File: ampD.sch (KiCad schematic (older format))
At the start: 13 parts, among them U10 Mux, U11 screw_term, U6 TL084, U9 screw_term

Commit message: changed to mcp6004 op amp
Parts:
- removed U6: TL084, Package_DIP:DIP-14_W7.62mm, symbol Amplifier_Operational:TL084
- added U6: MCP6004, Package_DIP:DIP-14_W7.62mm, symbol Amplifier_Operational:MCP6004
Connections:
- net out: now also U6.14
- net at R34.1, R35.1: now also U6.13 (-)
- net at R33.2, R36.2: now also U6.12 (+)
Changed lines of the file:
@@
 $Descr A4 11693 8268
 encoding utf-8
-Sheet 9 11
+Sheet 5 11
 Title ""
 Date ""
@@
 AR Path="/6019DBCE/60198F27" Ref="#PWR032"  Part="1"
 AR Path="/601B4C19/60198F27" Ref="#PWR062"  Part="1"
-F 0 "#PWR062" H 1450 1850 50  0001 C CNN
+F 0 "#PWR032" H 1450 1850 50  0001 C CNN
 F 1 "GND" H 1455 1927 50  0000 C CNN
 F 2 "" H 1450 2100 50  0001 C CNN
@@
 AR Path="/6019DBCE/6015EF5C" Ref="R35"  Part="1"
 AR Path="/601B4C19/6015EF5C" Ref="R71"  Part="1"
-F 0 "R71" H 5520 4096 50  0000 L CNN
+F 0 "R35" H 5520 4096 50  0000 L CNN
 F 1 "15" H 5520 4005 50  0000 L CNN
 F 2 "Resistor_THT:R_Axial_DIN0204_L3.6mm_D1.6mm_P5.08mm_Horizontal" V 5380 4050 50  0001 C CNN
@@
 AR Path="/6019DBCE/6019E3A7" Ref="R36"  Part="1"
 AR Path="/601B4C19/6019E3A7" Ref="R72"  Part="1"
-F 0 "R72" V 5743 3250 50  0000 C CNN
+F 0 "R36" V 5743 3250 50  0000 C CNN
 F 1 "15" V 5834 3250 50  0000 C CNN
 F 2 "Resistor_THT:R_Axial_DIN0204_L3.6mm_D1.6mm_P5.08mm_Horizontal" V 5880 3250 50  0001 C CNN
@@
 AR Path="/6019DBCE/6019E3B2" Ref="R33"  Part="1"
 AR Path="/601B4C19/6019E3B2" Ref="R69"  Part="1"
-F 0 "R69" V 5307 3700 50  0000 C CNN
+F 0 "R33" V 5307 3700 50  0000 C CNN
 F 1 "1" V 5216 3700 50  0000 C CNN
 F 2 "Resistor_THT:R_Axial_DIN0204_L3.6mm_D1.6mm_P5.08mm_Horizontal" V 5030 3700 50  0001 C CNN
@@
 AR Path="/6019DBCE/6019E3A8" Ref="R34"  Part="1"
 AR Path="/601B4C19/6019E3A8" Ref="R70"  Part="1"
-F 0 "R70" V 5000 3900 50  0000 C CNN
+F 0 "R34" V 5000 3900 50  0000 C CNN
 F 1 "1" V 4900 3900 50  0000 C CNN
 F 2 "Resistor_THT:R_Axial_DIN0204_L3.6mm_D1.6mm_P5.08mm_Horizontal" V 5030 3900 50  0001 C CNN
@@
 AR Path="/6019DBCE/6019E3B3" Ref="R31"  Part="1"
 AR Path="/601B4C19/6019E3B3" Ref="R67"  Part="1"
-F 0 "R67" H 3320 3546 50  0000 L CNN
+F 0 "R31" H 3320 3546 50  0000 L CNN
 F 1 "330" H 3320 3455 50  0000 L CNN
 F 2 "Resistor_THT:R_Axial_DIN0204_L3.6mm_D1.6mm_P5.08mm_Horizontal" V 3180 3500 50  0001 C CNN
@@
 AR Path="/6019DBCE/60198F36" Ref="R32"  Part="1"
 AR Path="/601B4C19/60198F36" Ref="R68"  Part="1"
-F 0 "R68" H 3320 3846 50  0000 L CNN
+F 0 "R32" H 3320 3846 50  0000 L CNN
 F 1 "560" H 3320 3755 50  0000 L CNN
 F 2 "Resistor_THT:R_Axial_DIN0204_L3.6mm_D1.6mm_P5.08mm_Horizontal" V 3180 3800 50  0001 C CNN
@@
 AR Path="/6019DBCE/60198F37" Ref="#PWR035"  Part="1"
 AR Path="/601B4C19/60198F37" Ref="#PWR065"  Part="1"
-F 0 "#PWR065" H 3250 3200 50  0001 C CNN
+F 0 "#PWR035" H 3250 3200 50  0001 C CNN
 F 1 "+3.3V" H 3265 3523 50  0000 C CNN
 F 2 "" H 3250 3350 50  0001 C CNN
@@
 AR Path="/6019DBCE/6019E3A9" Ref="#PWR036"  Part="1"
 AR Path="/601B4C19/6019E3A9" Ref="#PWR066"  Part="1"
-F 0 "#PWR066" H 3250 3700 50  0001 C CNN
+F 0 "#PWR036" H 3250 3700 50  0001 C CNN
 F 1 "GND" H 3255 3777 50  0000 C CNN
 F 2 "" H 3250 3950 50  0001 C CNN
@@
 AR Path="/6019DBCE/60198F29" Ref="#PWR037"  Part="1"
 AR Path="/601B4C19/60198F29" Ref="#PWR067"  Part="1"
-F 0 "#PWR067" H 5450 3950 50  0001 C CNN
+F 0 "#PWR037" H 5450 3950 50  0001 C CNN
 F 1 "GND" H 5455 4027 50  0000 C CNN
 F 2 "" H 5450 4200 50  0001 C CNN
@@
 AR Path="/6019DBCE/6019E3AD" Ref="R28"  Part="1"
 AR Path="/601B4C19/6019E3AD" Ref="R64"  Part="1"
-F 0 "R64" H 1520 1996 50  0000 L CNN
+F 0 "R28" H 1520 1996 50  0000 L CNN
 F 1 "330" H 1520 1905 50  0000 L CNN
 F 2 "Resistor_THT:R_Axial_DIN0204_L3.6mm_D1.6mm_P5.08mm_Horizontal" V 1380 1950 50  0001 C CNN
@@
 AR Path="/6019DBCE/6019E3AF" Ref="#PWR033"  Part="1"
 AR Path="/601B4C19/6019E3AF" Ref="#PWR063"  Part="1"
-F 0 "#PWR063" H 1450 2800 50  0001 C CNN
+F 0 "#PWR033" H 1450 2800 50  0001 C CNN
 F 1 "GND" H 1455 2877 50  0000 C CNN
 F 2 "" H 1450 3050 50  0001 C CNN
@@
 AR Path="/6019DBCE/6019E3AA" Ref="R29"  Part="1"
 AR Path="/601B4C19/6019E3AA" Ref="R65"  Part="1"
-F 0 "R65" H 1520 2946 50  0000 L CNN
+F 0 "R29" H 1520 2946 50  0000 L CNN
 F 1 "330" H 1520 2855 50  0000 L CNN
 F 2 "Resistor_THT:R_Axial_DIN0204_L3.6mm_D1.6mm_P5.08mm_Horizontal" V 1380 2900 50  0001 C CNN
@@
 AR Path="/6019DBCE/6019E3B1" Ref="#PWR034"  Part="1"
 AR Path="/601B4C19/6019E3B1" Ref="#PWR064"  Part="1"
-F 0 "#PWR064" H 1450 3800 50  0001 C CNN
+F 0 "#PWR034" H 1450 3800 50  0001 C CNN
 F 1 "GND" H 1455 3877 50  0000 C CNN
 F 2 "" H 1450 4050 50  0001 C CNN
@@
 AR Path="/6019DBCE/60198F3A" Ref="R30"  Part="1"
 AR Path="/601B4C19/60198F3A" Ref="R66"  Part="1"
-F 0 "R66" H 1520 3946 50  0000 L CNN
+F 0 "R30" H 1520 3946 50  0000 L CNN
 F 1 "330" H 1520 3855 50  0000 L CNN
 F 2 "Resistor_THT:R_Axial_DIN0204_L3.6mm_D1.6mm_P5.08mm_Horizontal" V 1380 3900 50  0001 C CNN
@@
 AR Path="/6019DBCE/6019A6B5" Ref="U11"  Part="2"
 AR Path="/601B4C19/6019A6B5" Ref="U20"  Part="2"
-F 0 "U20" H 1508 3884 50  0000 L CNN
+F 0 "U11" H 1508 3884 50  0000 L CNN
 F 1 "screw_term" H 1508 3793 50  0000 L CNN
 F 2 "Connector_PinHeader_1.27mm:PinHeader_1x02_P1.27mm_Vertical" H 1450 3750 50  0001 C CNN
@@
 AR Path="/6019DBCE/6019E3B7" Ref="U9"  Part="2"
 AR Path="/601B4C19/6019E3B7" Ref="U18"  Part="2"
-F 0 "U18" H 1508 1934 50  0000 L CNN
+F 0 "U9" H 1508 1934 50  0000 L CNN
 F 1 "screw_term" H 1508 1843 50  0000 L CNN
 F 2 "Connector_PinHeader_1.27mm:PinHeader_1x02_P1.27mm_Vertical" H 1450 1800 50  0001 C CNN
@@
 AR Path="/6019DBCE/6019E3B0" Ref="U11"  Part="1"
 AR Path="/601B4C19/6019E3B0" Ref="U20"  Part="1"
-F 0 "U20" H 1508 2884 50  0000 L CNN
+F 0 "U11" H 1508 2884 50  0000 L CNN
 F 1 "screw_term" H 1508 2793 50  0000 L CNN
 F 2 "Connector_PinHeader_1.27mm:PinHeader_1x02_P1.27mm_Vertical" H 1450 2750 50  0001 C CNN
@@
 	1    1450 2750
 	1    0    0    -1
-$EndComp
-$Comp
-L Amplifier_Operational:TL084 U?
-U 4 1 6017E42E
-P 6000 3800
-AR Path="/60132BC3/6013AE22/6017E42E" Ref="U?"  Part="1"
-AR Path="/6017CC5E/6017E42E" Ref="U?"  Part="1"
-AR Path="/6017DA21/6017E42E" Ref="U?"  Part="1"
-AR Path="/601927EB/6017E42E" Ref="U?"  Part="2"
-AR Path="/6019DBCE/6017E42E" Ref="U6"  Part="4"
-AR Path="/601B4C19/6017E42E" Ref="U15"  Part="4"
-F 0 "U15" H 6000 3433 50  0000 C CNN
-F 1 "TL084" H 6000 3524 50  0000 C CNN
-F 2 "Package_DIP:DIP-14_W7.62mm" H 5950 3900 50  0001 C CNN
-F 3 "http://www.ti.com/lit/ds/symlink/tl081.pdf" H 6050 4000 50  0001 C CNN
-	4    6000 3800
-	1    0    0    1
 $EndComp
 $Comp
@@
 AR Path="/6019DBCE/6017A5CD" Ref="U10"  Part="2"
 AR Path="/601B4C19/6017A5CD" Ref="U19"  Part="2"
-F 0 "U19" H 3375 2515 50  0000 C CNN
+F 0 "U10" H 3375 2515 50  0000 C CNN
 F 1 "Mux" H 3375 2424 50  0000 C CNN
 F 2 "Package_DIP:DIP-16_W7.62mm" H 3350 2050 50  0001 C CNN
@@
 	1    0    0    -1
 $EndComp
+$Comp
+L Amplifier_Operational:MCP6004 U6
+U 4 1 6018F24E
+P 6000 3800
+AR Path="/6019DBCE/6018F24E" Ref="U6"  Part="4"
+AR Path="/601B4C19/6018F24E" Ref="U15"  Part="4"
+F 0 "U6" H 6000 4167 50  0000 C CNN
+F 1 "MCP6004" H 6000 4076 50  0000 C CNN
+F 2 "Package_DIP:DIP-14_W7.62mm" H 5950 3900 50  0001 C CNN
+F 3 "http://ww1.microchip.com/downloads/en/DeviceDoc/21733j.pdf" H 6050 4000 50  0001 C CNN
+	4    6000 3800
+	1    0    0    -1
+$EndComp

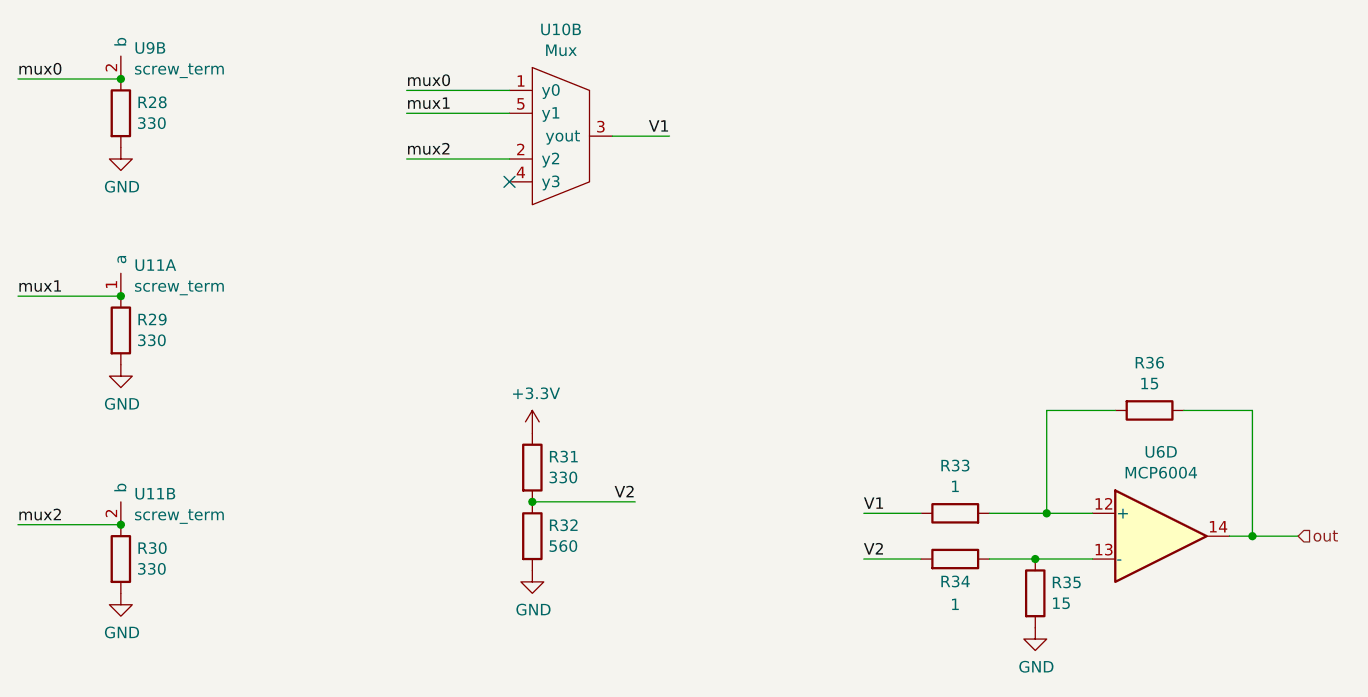
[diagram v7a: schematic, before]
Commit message: switched to sensor sheet for one sensor divider
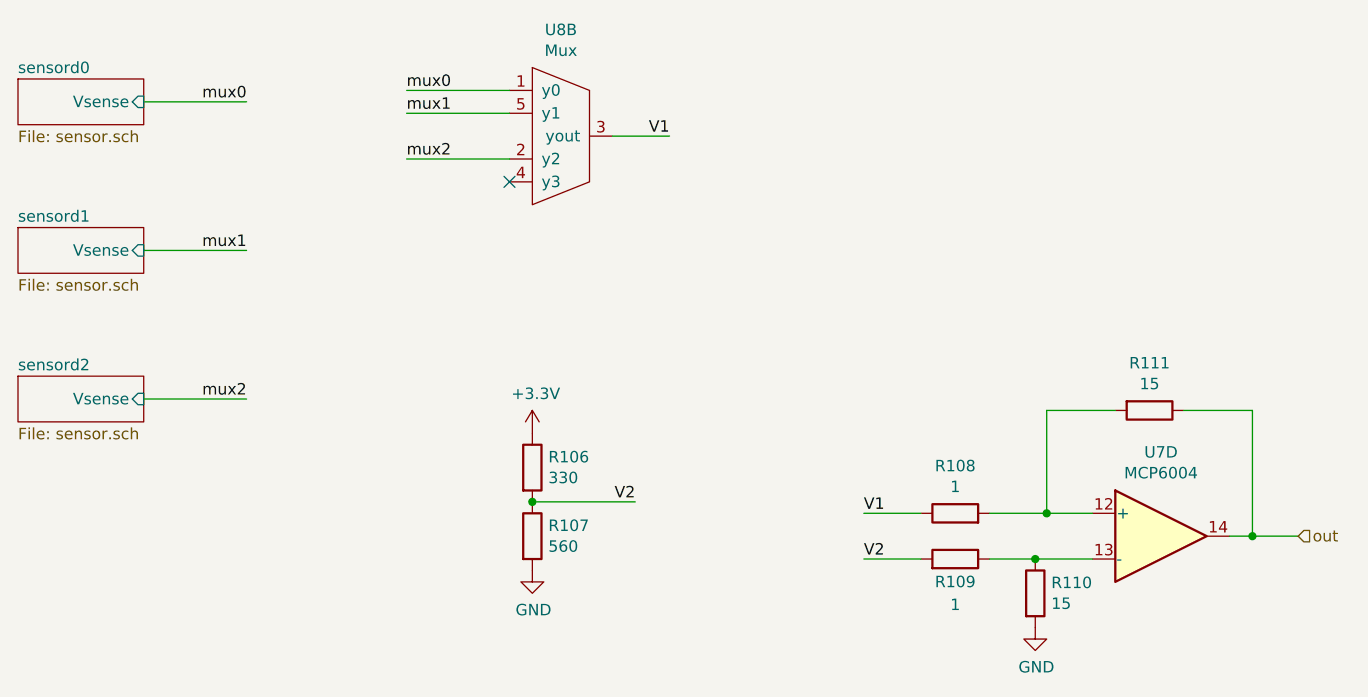
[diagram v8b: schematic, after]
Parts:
- removed R28, R29, R30: 330, Resistor_THT:R_Axial_DIN0204_L3.6mm_D1.6mm_P5.08mm_Horizontal, symbol Device:R
- removed U11, U9: screw_term, Connector_PinHeader_1.27mm:PinHeader_1x02_P1.27mm_Vertical, symbol PNG_PCB_Parts:screw_term
- renumbered R31 to R46, R32 to R47, R33 to R48, R34 to R49, R35 to R50, R36 to R51, U6 to U4, U10 to U5
